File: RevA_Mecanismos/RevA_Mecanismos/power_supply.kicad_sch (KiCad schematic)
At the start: 25 parts, among them Q2 NDS352AP, U2 R-78E3.3-1.0, U3 R-78E5.0-1.0

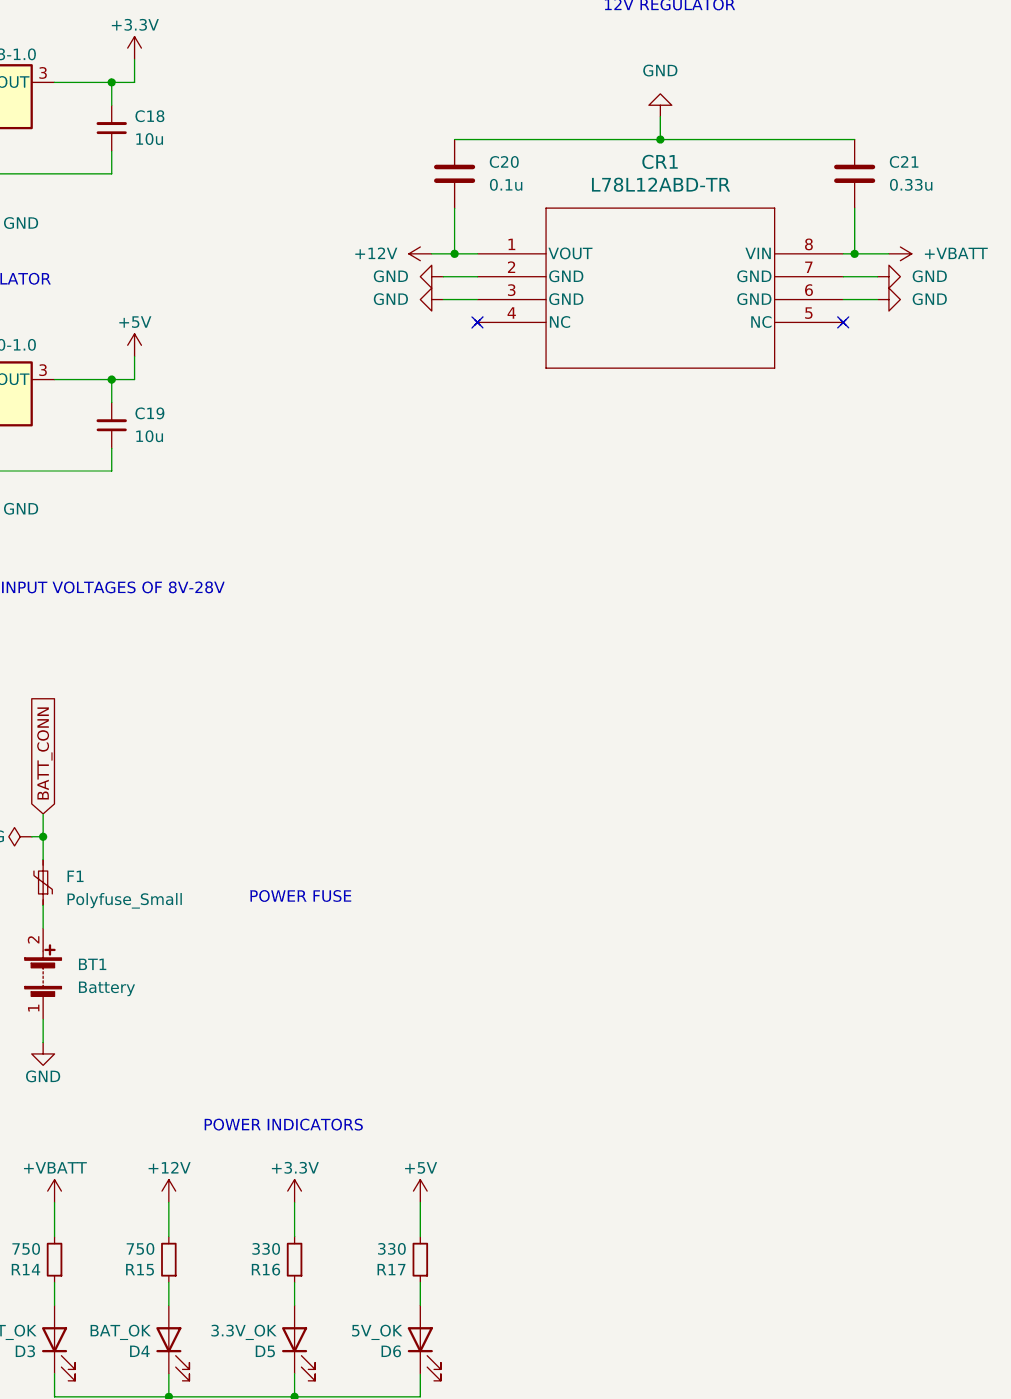
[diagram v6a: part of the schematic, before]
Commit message: Correction made to footprint for J3 pin header
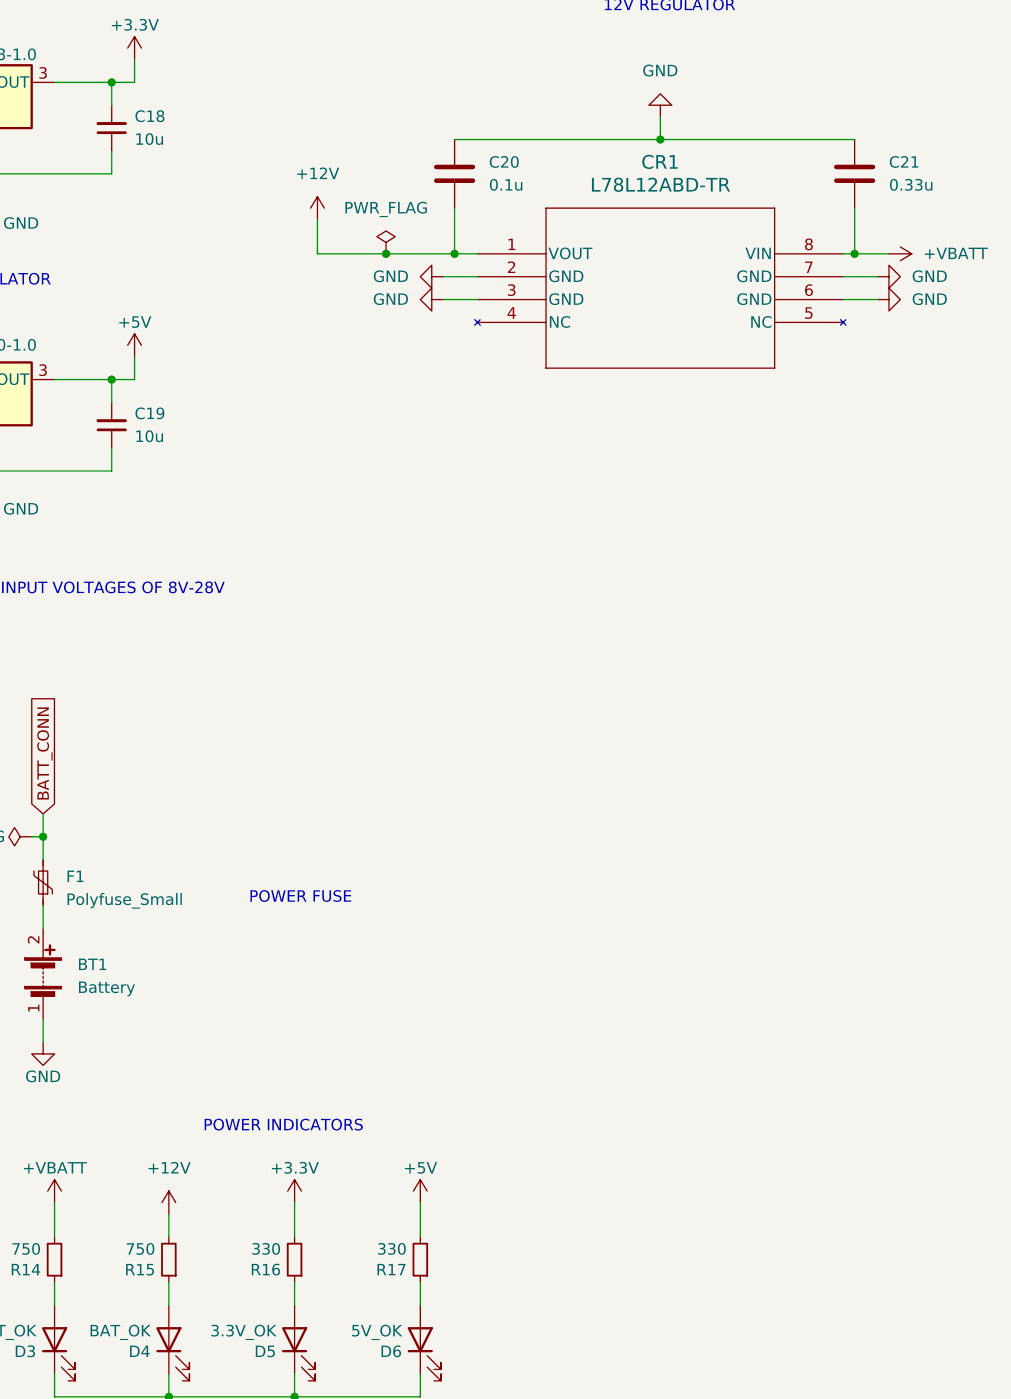
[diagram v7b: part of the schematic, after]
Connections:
- no-connect marks 2 -> 0
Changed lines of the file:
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@@
   (junction (at 132.08 35.56) (diameter 0) (color 0 0 0 0)
   )
+  (junction (at 162.56 54.61) (diameter 0) (color 0 0 0 0)
+  )
   (junction (at 54.61 173.99) (diameter 0) (color 0 0 0 0)
   )
@@
   (junction (at 193.04 41.91) (diameter 0) (color 0 0 0 0)
   )
-  (no_connect (at 213.36 62.23))
-  (no_connect (at 172.72 62.23))
   (wire (pts (xy 125.73 35.56) (xy 132.08 35.56))
     (stroke (width 0) (type default))
@@
     (stroke (width 0) (type default))
   )
-  (wire (pts (xy 167.64 54.61) (xy 170.18 54.61))
+  (wire (pts (xy 154.94 54.61) (xy 162.56 54.61))
     (stroke (width 0) (type default))
   )
@@
     (stroke (width 0) (type default))
   )
+  (wire (pts (xy 154.94 50.8) (xy 154.94 54.61))
+    (stroke (width 0) (type default))
+  )
   (wire (pts (xy 134.62 68.58) (xy 134.62 66.04))
     (stroke (width 0) (type default))
@@
   )
   (wire (pts (xy 54.61 173.99) (xy 54.61 175.26))
+    (stroke (width 0) (type default))
+  )
+  (wire (pts (xy 162.56 54.61) (xy 170.18 54.61))
     (stroke (width 0) (type default))
   )
@@
     (stroke (width 0) (type default))
   )
-  (wire (pts (xy 138.43 163.83) (xy 138.43 160.02))
+  (wire (pts (xy 138.43 161.29) (xy 138.43 163.83))
     (stroke (width 0) (type solid))
   )
@@
     )
   )
+  (symbol (lib_id "power:PWR_FLAG") (at 162.56 54.61 0) (unit 1)
+    (in_bom yes) (on_board yes) (dnp no) (fields_autoplaced)
+    (property "Reference" "#FLG06" (at 162.56 52.705 0)
+      (effects (font (size 1.27 1.27)) hide)
+    )
+    (property "Value" "PWR_FLAG" (at 162.56 49.53 0)
+      (effects (font (size 1.27 1.27)))
+    )
+    (property "Footprint" "" (at 162.56 54.61 0)
+      (effects (font (size 1.27 1.27)) hide)
+    )
+    (property "Datasheet" "~" (at 162.56 54.61 0)
+      (effects (font (size 1.27 1.27)) hide)
+    )
+    (pin "1")
+    (instances
+      (project "RevA_Mecanismos"
+        (path "/3a16a434-10b7-49a8-988b-273362cb395e/9466c5e7-8595-42d4-852d-e47b24624149"
+          (reference "#FLG06") (unit 1)
+        )
+      )
+    )
+  )
   (symbol (lib_id "Device:LED") (at 166.37 175.26 90) (unit 1)
     (in_bom yes) (on_board yes) (dnp no)
@@
     )
   )
-  (symbol (lib_id "power:+12V") (at 167.64 54.61 90) (unit 1)
-    (in_bom yes) (on_board yes) (dnp no) (fields_autoplaced)
-    (property "Reference" "#PWR044" (at 171.45 54.61 0)
-      (effects (font (size 1.27 1.27)) hide)
-    )
-    (property "Value" "+12V" (at 163.83 54.61 90)
-      (effects (font (size 1.27 1.27)) (justify left))
-    )
-    (property "Footprint" "" (at 167.64 54.61 0)
-      (effects (font (size 1.27 1.27)) hide)
-    )
-    (property "Datasheet" "" (at 167.64 54.61 0)
-      (effects (font (size 1.27 1.27)) hide)
-    )
-    (pin "1")
-    (instances
-      (project "RevA_Mecanismos"
-        (path "/3a16a434-10b7-49a8-988b-273362cb395e/9466c5e7-8595-42d4-852d-e47b24624149"
-          (reference "#PWR044") (unit 1)
-        )
-      )
-    )
-  )
   (symbol (lib_id "Device:C_Small") (at 104.14 40.64 180) (unit 1)
     (in_bom yes) (on_board yes) (dnp no) (fields_autoplaced)
@@
     )
   )
+  (symbol (lib_id "power:+12V") (at 154.94 50.8 0) (unit 1)
+    (in_bom yes) (on_board yes) (dnp no) (fields_autoplaced)
+    (property "Reference" "#PWR079" (at 154.94 54.61 0)
+      (effects (font (size 1.27 1.27)) hide)
+    )
+    (property "Value" "+12V" (at 154.94 45.72 0)
+      (effects (font (size 1.27 1.27)))
+    )
+    (property "Footprint" "" (at 154.94 50.8 0)
+      (effects (font (size 1.27 1.27)) hide)
+    )
+    (property "Datasheet" "" (at 154.94 50.8 0)
+      (effects (font (size 1.27 1.27)) hide)
+    )
+    (pin "1")
+    (instances
+      (project "RevA_Mecanismos"
+        (path "/3a16a434-10b7-49a8-988b-273362cb395e/9466c5e7-8595-42d4-852d-e47b24624149"
+          (reference "#PWR079") (unit 1)
+        )
+      )
+    )
+  )
   (symbol (lib_id "Device:C") (at 170.18 45.72 0) (unit 1)
     (in_bom yes) (on_board yes) (dnp no) (fields_autoplaced)
@@
     )
   )
-  (symbol (lib_id "power:+12V") (at 138.43 160.02 0) (unit 1)
-    (in_bom yes) (on_board yes) (dnp no)
-    (property "Reference" "#PWR040" (at 138.43 163.83 0)
+  (symbol (lib_id "power:+12V") (at 138.43 161.29 0) (unit 1)
+    (in_bom yes) (on_board yes) (dnp no) (fields_autoplaced)
+    (property "Reference" "#PWR040" (at 138.43 165.1 0)
       (effects (font (size 1.27 1.27)) hide)
     )
@@
       (effects (font (size 1.27 1.27)))
     )
-    (property "Footprint" "" (at 138.43 160.02 0)
-      (effects (font (size 1.27 1.27)) hide)
-    )
-    (property "Datasheet" "" (at 138.43 160.02 0)
-      (effects (font (size 1.27 1.27)) hide)
-    )
+    (property "Footprint" "" (at 138.43 161.29 0)
+      (effects (font (size 1.27 1.27)) hide)
+    )
+    (property "Datasheet" "" (at 138.43 161.29 0)
+      (effects (font (size 1.27 1.27)) hide)
+    )
